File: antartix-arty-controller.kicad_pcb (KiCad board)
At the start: 4 copper layers, 96 x 40 mm, 168 parts, among them IC1 FT2232D, IC2 TPD8S009DSMR, J1 QTE-020-04-L-D-A, J10 3-794680-8, J11 1-794610-1, J12 1-794610-1, J13 1-794610-1, J14 1-794610-1, J15 3-794617-8, J16 1-794610-1, J17 1-794610-1, J18 1-794610-1, J19 1-794610-1, J2 0022232041, J3 614004185023, J4 WE_629105150521, J5 614004185023, J6 614004185023, J7 QTE-020-04-L-D-A, J8 WE_629105150521, J9 WE_685119136923, Q1 FDC6330L, Q2 FDC6330L, Q3 FDC6330L, U1 PCT2075GVX, U2 PAC1934T-I_JQ, U3 USB2514B-I_M2, U4 TPS2024DR, U5 TPS2024DR, U6 TPS2024DR, U7 FT230XS-R, Y1 7C-24.000MBB-T, Y2 MQ-6.000-12-30_30_

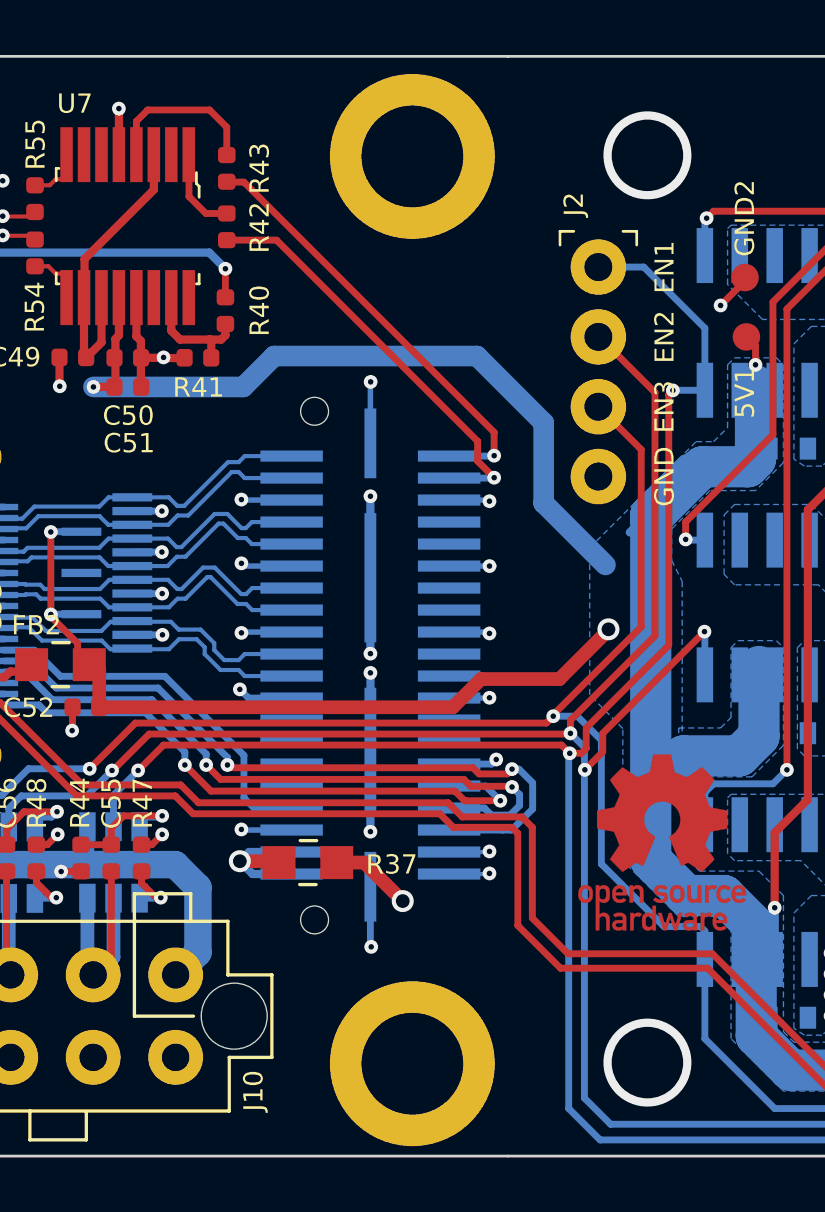
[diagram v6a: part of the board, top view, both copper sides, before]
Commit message: Remove redundant spacers and 3D model of additional conenctor
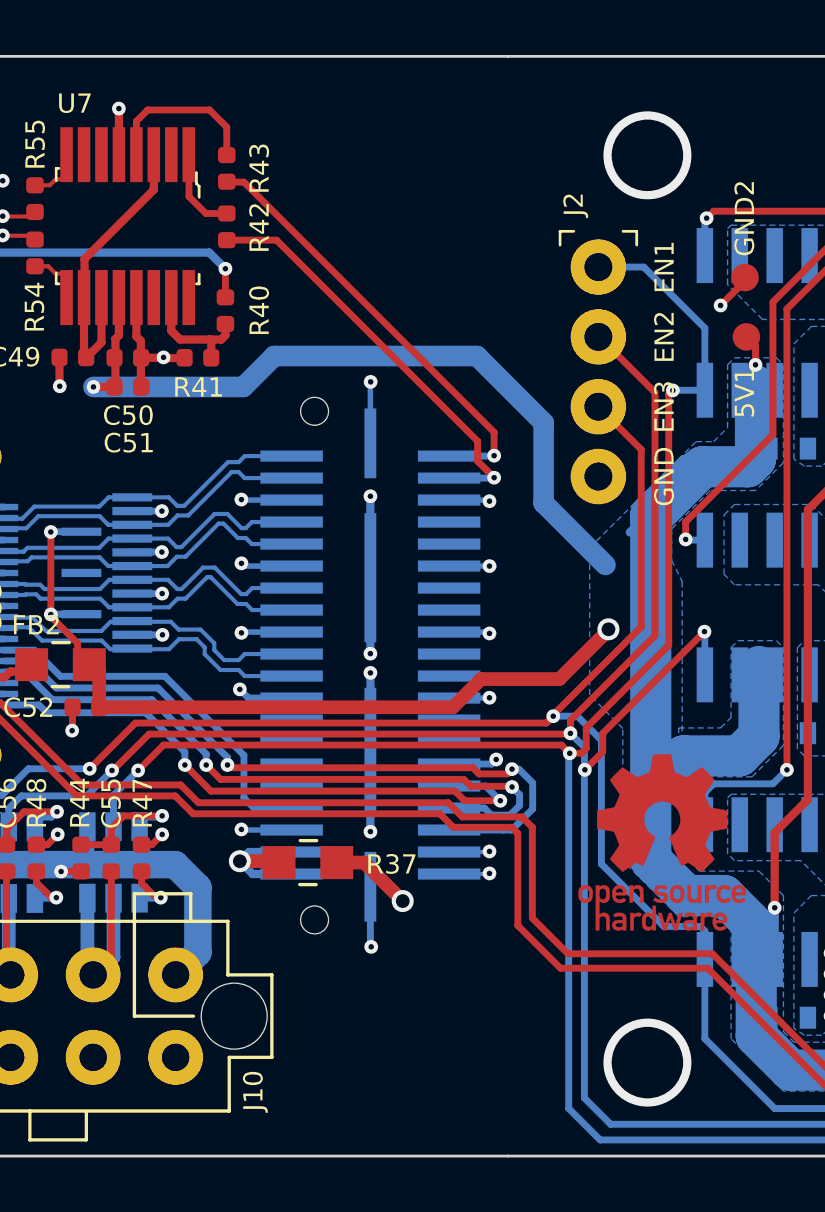
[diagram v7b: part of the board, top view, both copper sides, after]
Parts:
- removed SP1, SP2: 9774030151, antmicro-footprints:9774030151
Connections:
- net RXD1 renamed Net-(IC1-Pad39)
- net TXD1 renamed Net-(IC1-Pad40)

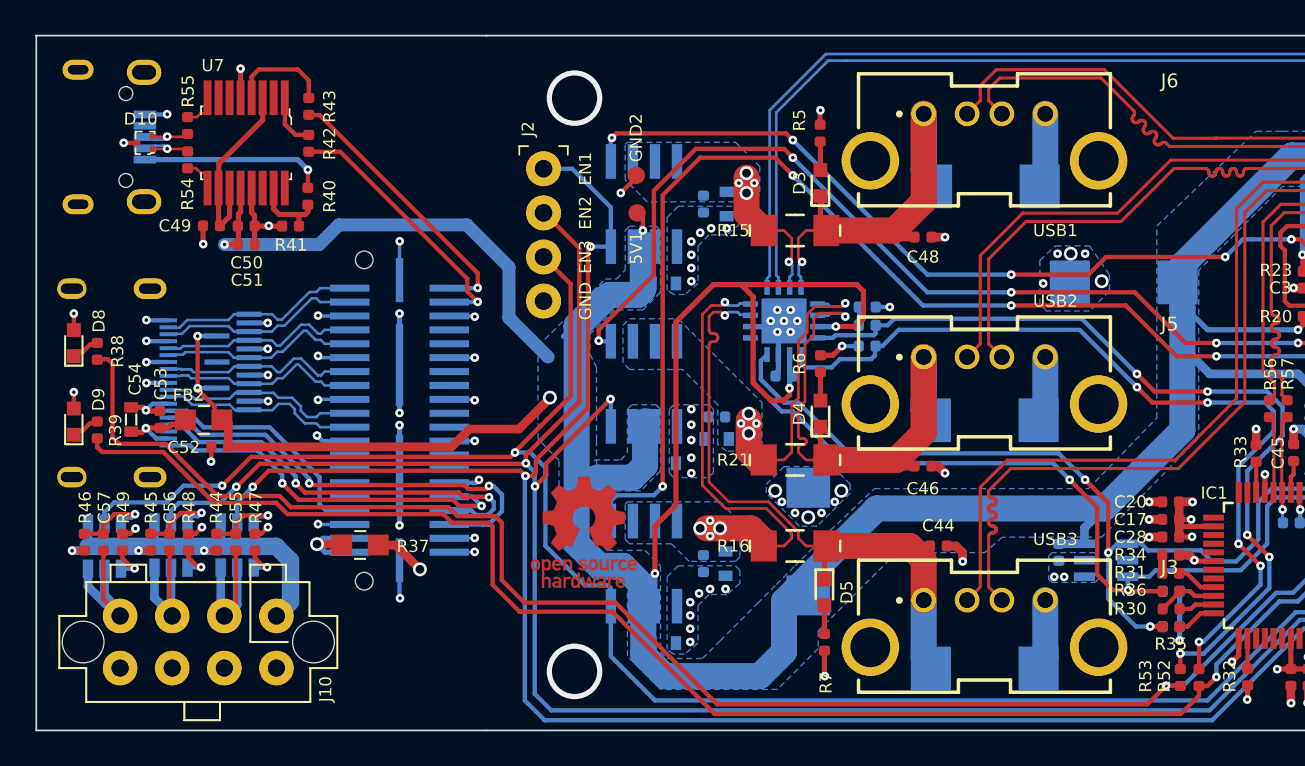
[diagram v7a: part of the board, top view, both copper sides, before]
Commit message: Redesign HDMI and Micro USB layout
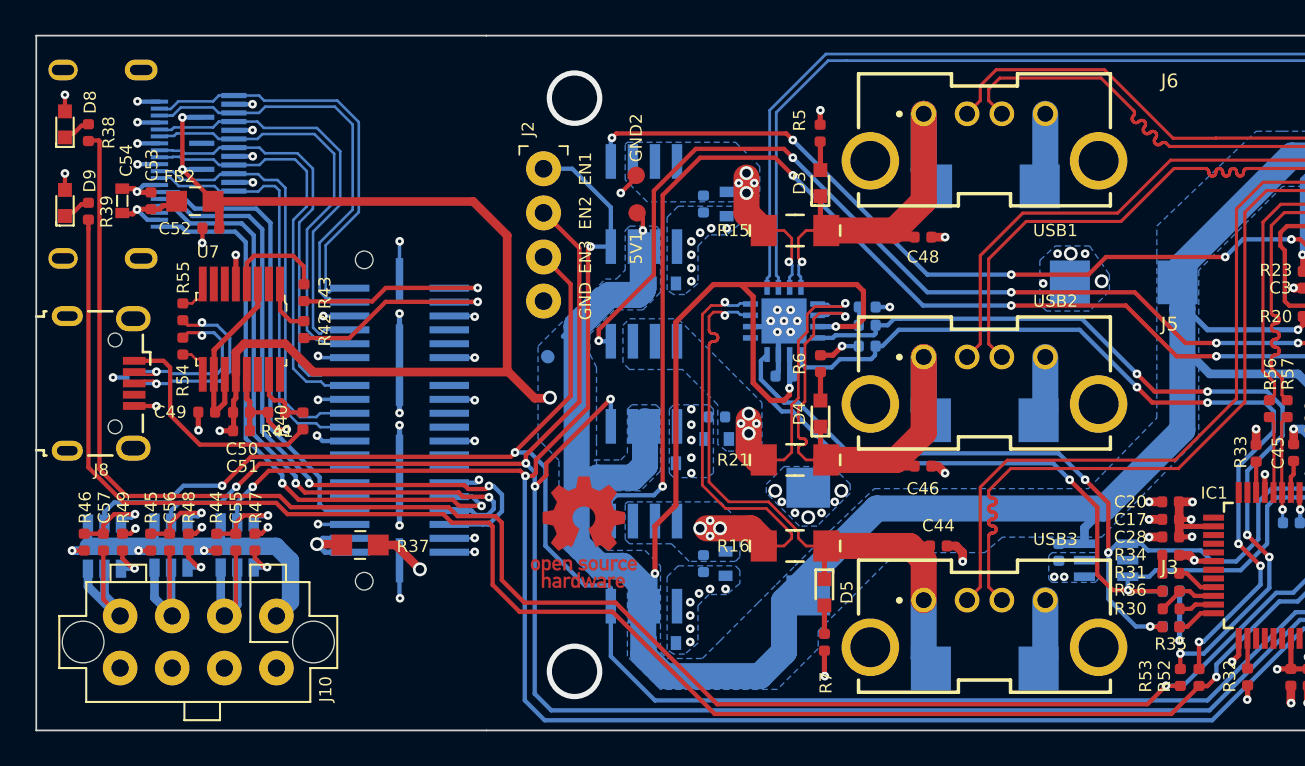
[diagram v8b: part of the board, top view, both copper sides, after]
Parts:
- D10: moved to B.Cu
- J8: moved to F.Cu
- moved J8 14.2 mm to (145.7, 92.5), turned to 270 degrees
- moved D10 13.5 mm to (147.6, 92.2), turned to 270 degrees
- moved R40 12.9 mm to (157.3, 94.7), turned to 90 degrees
- moved IC2 12.6 mm to (151.6, 78.7)
- moved C52 12.6 mm to (152.1, 83.6)
- moved C53 12.6 mm to (148.6, 82.0)
- moved C54 12.6 mm to (147.0, 82.0)
- moved D9 12.6 mm to (143.7, 82.1)
- moved FB2 12.6 mm to (151.1, 82.0)
- moved J9 12.6 mm to (145.5, 79.9)
- moved R38 12.6 mm to (145.0, 78.1)
- moved D8 12.6 mm to (143.7, 77.6)
- moved R39 12.6 mm to (145.0, 82.6)
- moved R41 10.8 mm to (155.8, 94.2)
- moved C49 10.7 mm to (151.8, 94.2)
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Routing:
- net LED0: track 103.0 -> 117.3 mm
- net LED1: track 99.0 -> 112.5 mm
- net HDMI0_D1_P: track 11.6 -> 24.5 mm
- net HDMI0_D0_N: track 11.6 -> 24.5 mm
- net HDMI0_D0_P: track 11.6 -> 24.4 mm
- net HDMI0_D1_N: track 11.6 -> 24.4 mm
- net HDMI0_CK_P: track 11.6 -> 24.4 mm
- net HDMI0_CK_N: track 11.6 -> 24.4 mm
- net HDMI0_D2_N: track 11.7 -> 24.4 mm
- net HDMI0_D2_P: track 11.7 -> 24.4 mm
- net HDMI0_CEC: track 13.8 -> 26.4 mm
- net HDMI0_SCL: track 25.7 -> 38.2 mm
- net HDMI0_SDA: track 24.0 -> 36.5 mm
- net HDMI0_HOTPLUG: track 21.8 -> 34.2 mm
- net /antartix hdmi adapter/USB_CON_P: track 3.39 -> 12.0 mm, vias 1 -> 2
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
